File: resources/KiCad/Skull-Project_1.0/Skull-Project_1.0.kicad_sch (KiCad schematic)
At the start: 7 parts, among them SW1 SW_SPST, SW2 SW_SPST

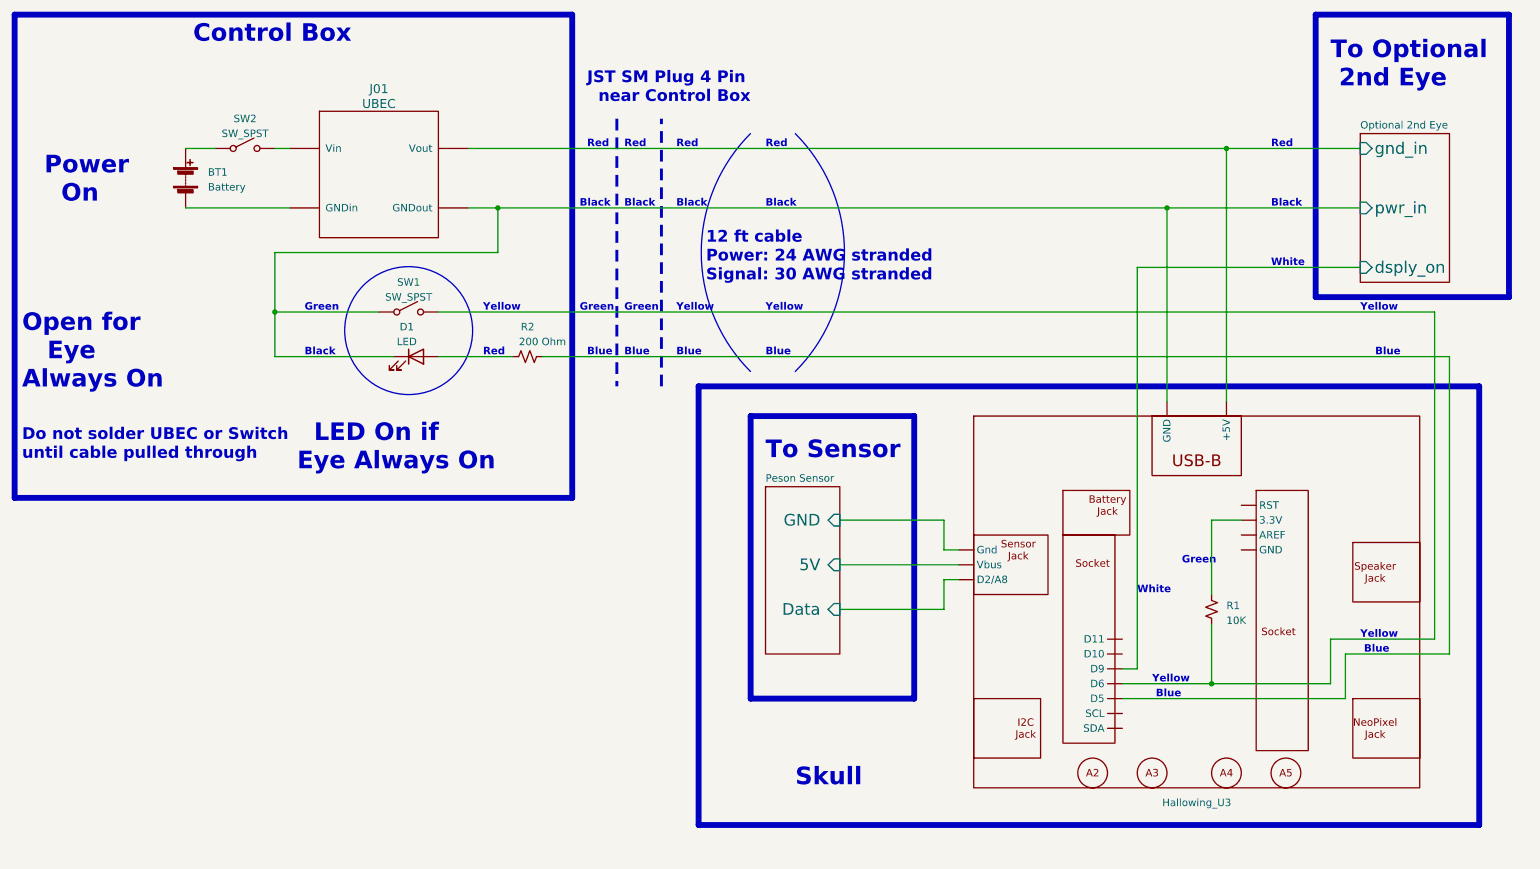
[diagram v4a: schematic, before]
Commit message: schematic uses 4pin cable for power, details on internal skull cabling
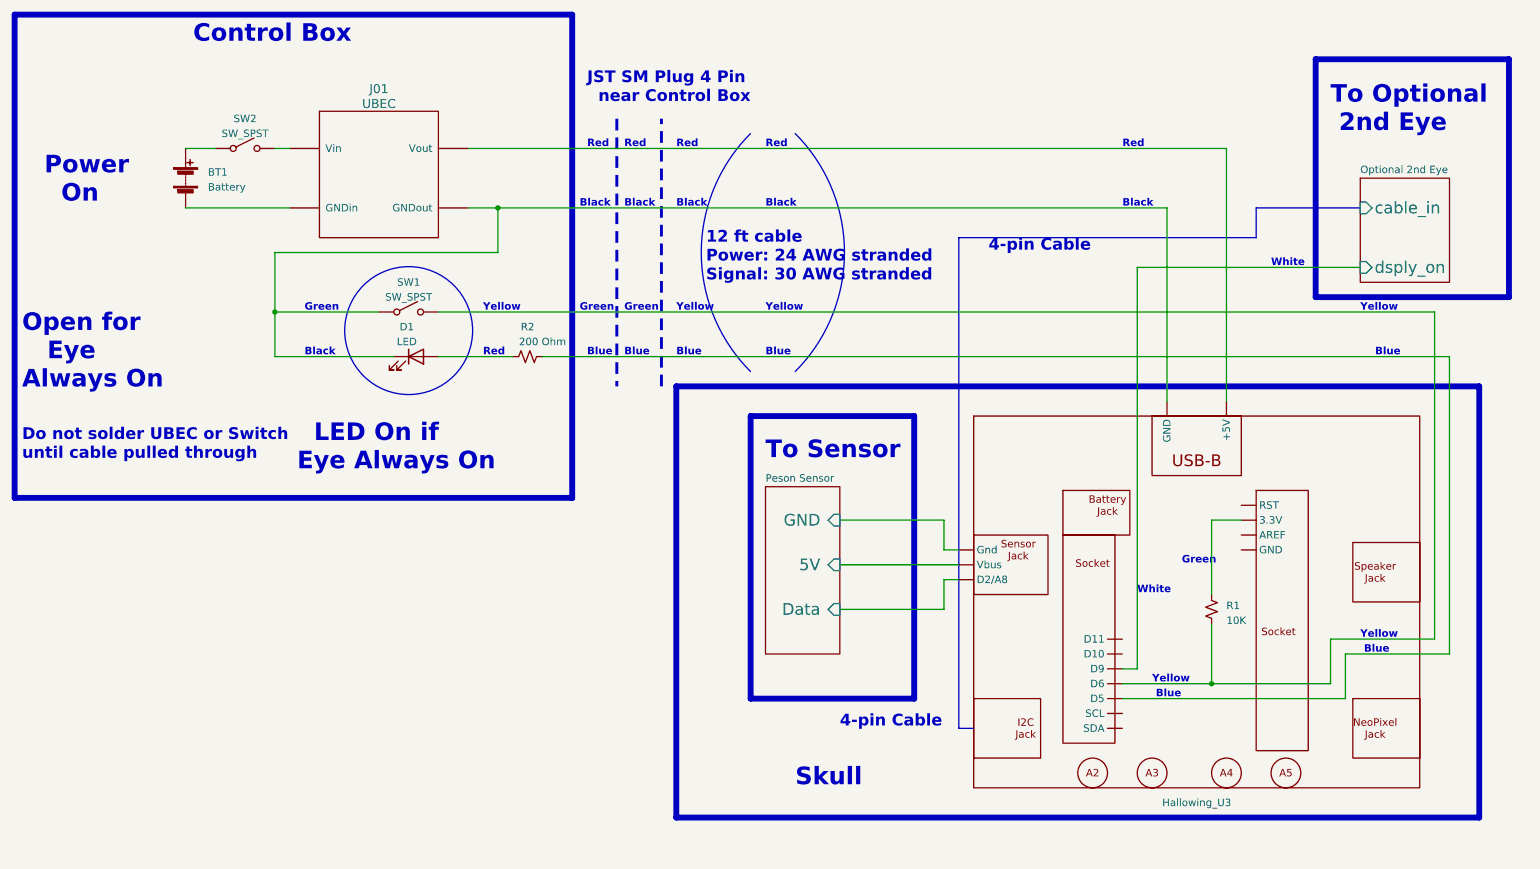
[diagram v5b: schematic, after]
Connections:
- net Optional 2nd Eye/gnd_in is gone; now on net Peson Sensor/GND : Hallowing_U3. (Vbus)
- net at SW2.~ (B): now also BT1.1 (+)
- net Optional 2nd Eye/pwr_in: no longer names the net of D1.1 (K), Hallowing_U3. (Vbus), SW1.~ (B)
- new net: Hallowing_U3. (Vbus), R1.2, SW1.~ (B)
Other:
- sheet Optional 2nd Eye ports: added cable_in ; removed gnd_in, pwr_in
- note added: "4-pin Cable"
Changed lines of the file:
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@@
   (title_block
     (title "Skull-Project 1.0")
-    (date "2024-09-20")
+    (date "2024-09-25")
     (rev "1.0")
     (company "github.com/Mark-MDO47/Skull-Project")
     (comment 2 "NOTE: Hallowing as from display side (not connector side)")
   )
-  (junction (at 213.36 53.34) (diameter 0) (color 0 0 0 0)
-  )
   (junction (at 220.98 134.62) (diameter 0) (color 0 0 0 0)
-  )
-  (junction (at 223.52 43.18) (diameter 0) (color 0 0 0 0)
   )
   (junction (at 99.06 53.34) (diameter 0) (color 0 0 0 0)
@@
     (stroke (width 0) (type default))
   )
+  (bus (pts (xy 228.6 53.34) (xy 228.6 58.42))
+    (stroke (width 0) (type default))
+  )
   (wire (pts (xy 45.72 53.34) (xy 63.5 53.34))
     (stroke (width 0) (type default))
   )
+  (bus (pts (xy 246.38 53.34) (xy 228.6 53.34))
+    (stroke (width 0) (type default))
+  )
   (wire (pts (xy 208.28 63.5) (xy 246.38 63.5))
     (stroke (width 0) (type default))
@@
     (stroke (width 0) (type default))
   )
-  (wire (pts (xy 213.36 53.34) (xy 246.38 53.34))
-    (stroke (width 0) (type default))
-  )
-  (wire (pts (xy 223.52 43.18) (xy 246.38 43.18))
+  (bus (pts (xy 177.8 58.42) (xy 177.8 142.24))
     (stroke (width 0) (type default))
   )
@@
     (stroke (width 0) (type default))
   )
+  (bus (pts (xy 228.6 58.42) (xy 177.8 58.42))
+    (stroke (width 0) (type default))
+  )
   (wire (pts (xy 88.9 71.12) (xy 259.08 71.12))
     (stroke (width 0) (type default))
   )
+  (bus (pts (xy 177.8 142.24) (xy 180.34 142.24))
+    (stroke (width 0) (type default))
+  )
   (wire (pts (xy 223.52 43.18) (xy 223.52 86.36))
     (stroke (width 0) (type default))
@@
     (fill (type none))
   )
-  (rectangle (start 238.76 20.32) (end 271.78 68.58)
+  (rectangle (start 238.76 27.94) (end 271.78 68.58)
     (stroke (width 1) (type default) (color 255 153 0 1))
     (fill (type none))
@@
     (fill (type none))
   )
-  (rectangle (start 133.35 83.82) (end 266.7 158.75)
+  (rectangle (start 129.54 83.82) (end 266.7 157.48)
     (stroke (width 1) (type default))
     (fill (type none))
@@
     (effects (font (size 1.27 1.27) (thickness 0.254) bold) (justify left bottom))
   )
+  (text "4-pin Cable" (at 182.88 60.96 0)
+    (effects (font (size 2 2) bold) (justify left bottom))
+  )
   (text "White" (at 231.14 63.5 0)
     (effects (font (size 1.27 1.27) bold) (justify left bottom))
@@
     (effects (font (size 1.27 1.27) bold) (justify left bottom))
   )
-  (text "To Optional\n 2nd Eye" (at 241.3 33.02 0)
+  (text "To Optional\n 2nd Eye" (at 241.3 40.64 0)
     (effects (font (size 3 3) bold) (justify left bottom))
   )
@@
     (effects (font (size 1.27 1.27) bold) (justify left bottom))
   )
-  (text "Red" (at 231.14 43.18 0)
+  (text "Red" (at 205.74 43.18 0)
     (effects (font (size 1.27 1.27) bold) (justify left bottom))
   )
   (text "Black" (at 129.54 53.34 0)
     (effects (font (size 1.27 1.27) bold) (justify left bottom))
+  )
+  (text "4-pin Cable" (at 157.48 142.24 0)
+    (effects (font (size 2 2) bold) (justify left bottom))
   )
   (text "Blue" (at 120.65 78.74 0)
@@
     (effects (font (size 1.27 1.27) bold) (justify left bottom))
   )
-  (text "Black" (at 231.14 53.34 0)
+  (text "Black" (at 205.74 53.34 0)
     (effects (font (size 1.27 1.27) bold) (justify left bottom))
   )
@@
     )
   )
-  (sheet (at 246.38 40.64) (size 15.24 25.4) (fields_autoplaced)
+  (sheet (at 246.38 48.26) (size 15.24 17.78) (fields_autoplaced)
     (stroke (width 0.1524) (type solid))
     (fill (color 0 0 0 0.0000))
-    (property "Sheetname" "Optional 2nd Eye" (at 246.38 39.9284 0)
+    (property "Sheetname" "Optional 2nd Eye" (at 246.38 47.5484 0)
       (effects (font (size 1.27 1.27)) (justify left bottom))
     )
@@
       (effects (font (size 1.27 1.27)) (justify left top) hide)
     )
-    (pin "gnd_in" input (at 246.38 43.18 180)
-      (effects (font (size 2 2)) (justify left))
-    )
-    (pin "pwr_in" input (at 246.38 53.34 180)
-      (effects (font (size 2 2)) (justify left))
-    )
     (pin "dsply_on " input (at 246.38 63.5 180)
       (effects (font (size 2 2)) (justify left))
     )
+    (pin "cable_in " input (at 246.38 53.34 180)
+      (effects (font (size 2 2)) (justify left))
+    )

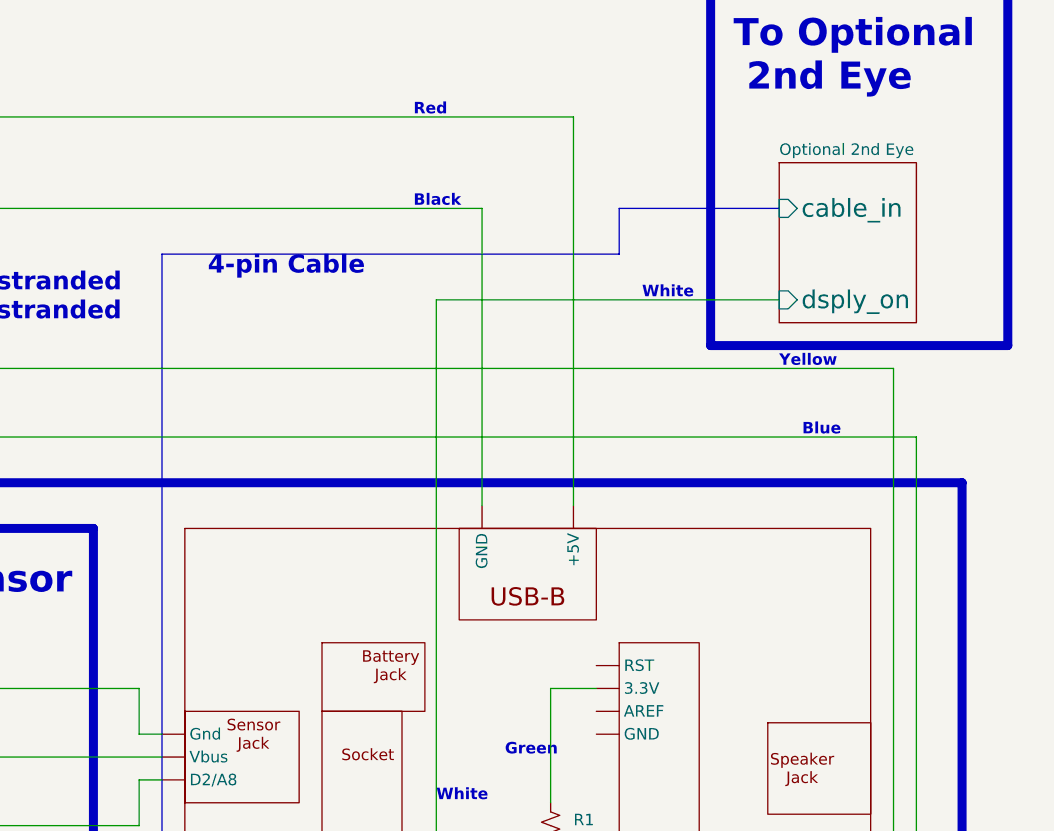
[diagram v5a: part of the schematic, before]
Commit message: add rst-2-prim to schematic
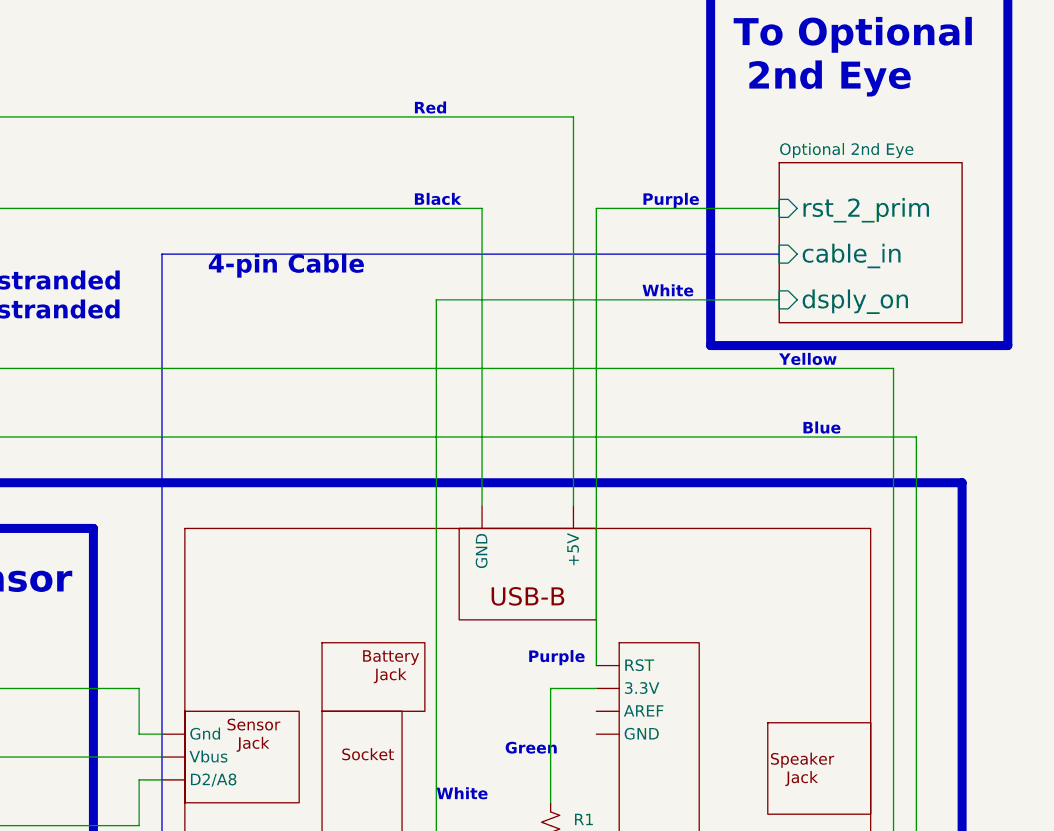
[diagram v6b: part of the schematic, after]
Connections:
- net at SW2.~ (B): now also BT1.1 (+)
- new net: Hallowing_U3. (Vbus), R1.2, SW1.~ (B)
- new net Optional 2nd Eye/rst_2_prim: Hallowing_U3. (Vbus)
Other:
- sheet Optional 2nd Eye ports: added rst_2_prim; removed none
- note added: "Purple"
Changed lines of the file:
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@@
   (title_block
     (title "Skull-Project 1.0")
-    (date "2024-09-25")
+    (date "2024-09-27")
     (rev "1.0")
     (company "github.com/Mark-MDO47/Skull-Project")
@@
     (stroke (width 0) (type default))
   )
+  (wire (pts (xy 226.06 53.34) (xy 246.38 53.34))
+    (stroke (width 0) (type default))
+  )
   (wire (pts (xy 175.26 116.84) (xy 175.26 121.92))
     (stroke (width 0) (type default))
@@
     (stroke (width 0) (type default))
   )
-  (bus (pts (xy 228.6 53.34) (xy 228.6 58.42))
-    (stroke (width 0) (type default))
-  )
   (wire (pts (xy 45.72 53.34) (xy 63.5 53.34))
     (stroke (width 0) (type default))
   )
-  (bus (pts (xy 246.38 53.34) (xy 228.6 53.34))
+  (bus (pts (xy 177.8 58.42) (xy 246.38 58.42))
     (stroke (width 0) (type default))
   )
@@
     (stroke (width 0) (type default))
   )
-  (bus (pts (xy 228.6 58.42) (xy 177.8 58.42))
-    (stroke (width 0) (type default))
-  )
   (wire (pts (xy 88.9 71.12) (xy 259.08 71.12))
     (stroke (width 0) (type default))
@@
   )
   (wire (pts (xy 205.74 134.62) (xy 220.98 134.62))
+    (stroke (width 0) (type default))
+  )
+  (wire (pts (xy 226.06 104.14) (xy 226.06 53.34))
     (stroke (width 0) (type default))
   )
@@
     (effects (font (size 1.27 1.27) (thickness 0.254) bold) (justify left bottom))
   )
+  (text "Purple" (at 218.44 104.14 0)
+    (effects (font (size 1.27 1.27) bold) (justify left bottom))
+  )
   (text "Blue" (at 129.54 78.74 0)
     (effects (font (size 1.27 1.27) bold) (justify left bottom))
@@
   )
   (text "Black" (at 66.04 78.74 0)
+    (effects (font (size 1.27 1.27) bold) (justify left bottom))
+  )
+  (text "Purple" (at 231.14 53.34 0)
     (effects (font (size 1.27 1.27) bold) (justify left bottom))
   )
@@
     )
   )
-  (sheet (at 246.38 48.26) (size 15.24 17.78) (fields_autoplaced)
+  (sheet (at 246.38 48.26) (size 20.32 17.78) (fields_autoplaced)
     (stroke (width 0.1524) (type solid))
     (fill (color 0 0 0 0.0000))
@@
       (effects (font (size 2 2)) (justify left))
     )
-    (pin "cable_in " input (at 246.38 53.34 180)
+    (pin "cable_in " input (at 246.38 58.42 180)
       (effects (font (size 2 2)) (justify left))
     )
+    (pin "rst_2_prim" input (at 246.38 53.34 180)
+      (effects (font (size 2 2)) (justify left))
+    )

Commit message: move schematic pdf to root directory + minor change
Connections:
- net at SW2.~ (B): now also BT1.1 (+)
- new net: Hallowing_U3. (Vbus), R1.2, SW1.~ (B)
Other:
- note added: "Do not solder UBEC or Switch until cable is pulled through"
- note removed: "Do not solder UBEC or Switch until cable pulled through"
- note removed: "Open for Eye Always On"
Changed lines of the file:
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@@
   (title_block
     (title "Skull-Project 1.0")
-    (date "2024-09-27")
+    (date "2024-09-28")
     (rev "1.0")
     (company "github.com/Mark-MDO47/Skull-Project")
@@
     (fill (type none))
   )
-  (rectangle (start 16.51 20.32) (end 111.76 102.87)
+  (rectangle (start 16.51 20.32) (end 111.76 88.9)
     (stroke (width 1) (type default))
     (fill (type none))
@@
     (effects (font (size 1.27 1.27) bold) (justify left bottom))
   )
-  (text "Do not solder UBEC or Switch\nuntil cable pulled through"
-    (at 17.78 96.52 0)
+  (text "Do not solder \nUBEC or Switch\nuntil cable is\npulled through"
+    (at 17.78 35.56 0)
     (effects (font (size 2 2) (thickness 0.4) bold) (justify left bottom))
   )
-  (text "Open for\n   Eye\nAlways On" (at 17.78 84.455 0)
-    (effects (font (size 3 3) (thickness 0.6) bold) (justify left bottom))
-  )
   (text "Blue" (at 247.015 129.54 0)
     (effects (font (size 1.27 1.27) bold) (justify left bottom))
@@
     (effects (font (size 3 3) (thickness 0.6) bold) (justify left bottom))
   )
-  (text "  LED On if\nEye Always On" (at 64.77 98.425 0)
-    (effects (font (size 3 3) (thickness 0.6) bold) (justify left bottom))
-  )
+  (text "  LED On if\nEye Always On" (at 20.32 73.66 0)
+    (effects (font (size 3 3) (thickness 0.6) bold) (justify left bottom))
+  )

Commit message: update to KiCad 8.0.7
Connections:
- net at SW2.~ (B): now also BT1.1 (+)
- new net: Hallowing_U3. (Vbus), R1.2, SW1.~ (B)
